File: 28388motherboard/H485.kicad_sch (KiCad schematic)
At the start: 23 parts, among them CN8 DB141V-2.54-6P, Q44 TPT75176B-SO1R, Q45 SN74LVC1G125DCKR

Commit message: 完成第一版引脚分配
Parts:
- removed D12, D34: ${MANUFACTURER PART}, 1mmlab_footprint:SOD-323_L1.8-W1.3-LS2.5-BI, symbol ESD:PESD12VL1BA,115
- added D20: SDT23C712L02_C5197393, Lib2ic:SOT-23-3_L2.9-W1.3-P1.90-LS2.4-BR, symbol sheet1-altium-import:SDT23C712L02_C5197393
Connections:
- net GND: now also D20.3
- net 485B: now reaches C181.1, L14.4, Q44.7 (B), R284.2, R296.1
- net 485B: now also D20.2
- net 485A: now reaches C182.1, L14.1, Q44.6 (A), R286.1, R296.2
- net 485A: now also D20.1

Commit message: 修改了一些bug，进行了一些布线
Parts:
- renumbered C170 to C25, C172 to C26, C174 to C27, C176 to C28, C179 to C29, C181 to C30, C182 to C31, CN8 to CN3, D20 to D14, L14 to L3, Q44 to Q10, Q45 to Q11, R272 to R34, R274 to R35, R276 to R36, R278 to R37, R281 to R38, R282 to R39, R284 to R40, R286 to R41, R295 to R42, R296 to R43

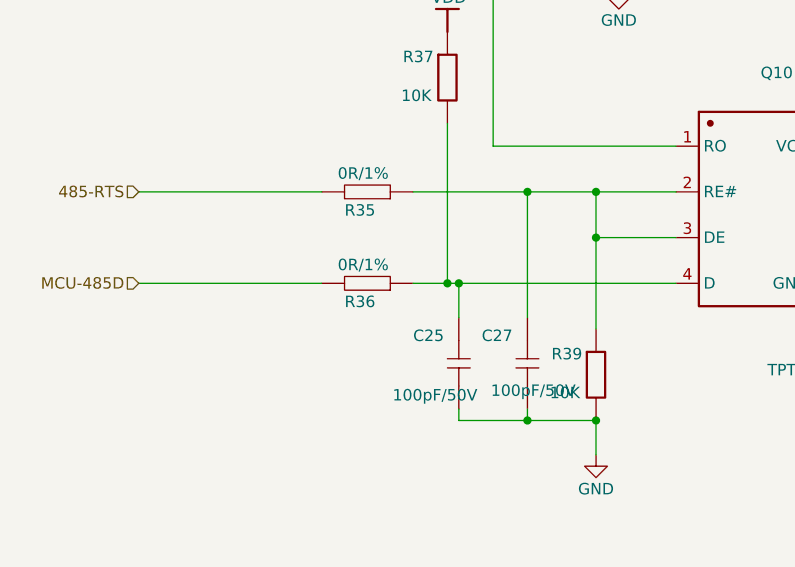
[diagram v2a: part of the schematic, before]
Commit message: 完成布局布线，需要丝印检查，原理图检查
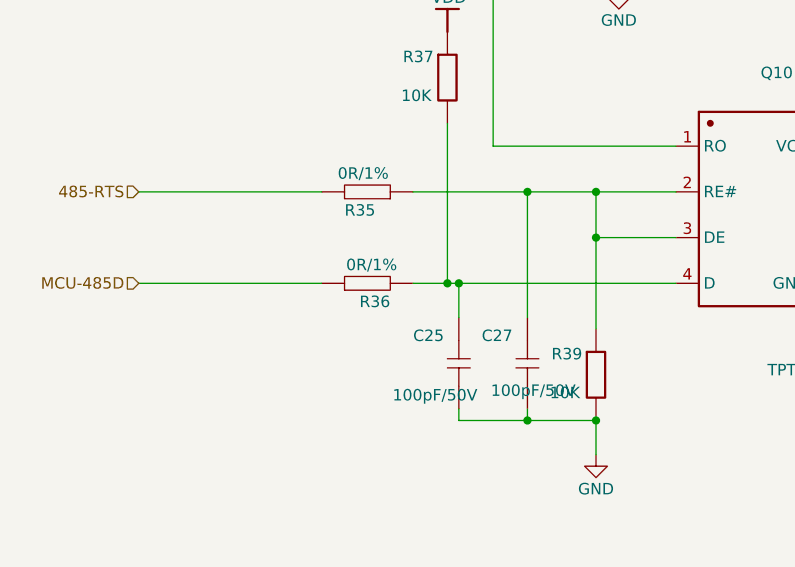
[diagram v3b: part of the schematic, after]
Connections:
- net MCU-485D: now also R36.1; no longer R36.2
- net at C25.1, Q10.4 (D), R37.2: now also R36.2; no longer R36.1
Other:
- moved on the sheet: R36
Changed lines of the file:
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@@
 	(wire
 		(pts
-			(xy 82.55 99.06) (xy 81.28 99.06)
-		)
-		(stroke
-			(width 0)
-			(type default)
-		)
-	)
-	(wire
-		(pts
 			(xy 115.57 48.26) (xy 100.33 48.26)
 		)
@@
 	(wire
 		(pts
+			(xy 81.28 99.06) (xy 82.55 99.06)
+		)
+		(stroke
+			(width 0)
+			(type default)
+		)
+	)
+	(wire
+		(pts
 			(xy 171.45 99.06) (xy 161.29 99.06)
 		)
@@
 	(symbol
 		(lib_id "sheet1-altium-import:RES_7")
-		(at 74.93 101.6 180)
+		(at 69.85 101.6 0)
+		(mirror x)
 		(unit 1)
 		(exclude_from_sim no)
@@
 		(dnp no)
 		(property "Reference" "R36"
-			(at 69.85 101.854 0)
+			(at 74.93 101.854 0)
 			(effects
 				(font
@@
 		)
 		(property "Value" "0R/1%"
-			(at 69.088 96.266 0)
+			(at 75.692 96.266 0)
 			(effects
 				(font
@@
 		)
 		(property "Footprint" "Resistor_SMD:R_0603_1608Metric"
-			(at 74.93 101.6 0)
+			(at 69.85 101.6 0)
 			(effects
 				(font
@@
 		)
 		(property "Datasheet" ""
-			(at 74.93 101.6 0)
+			(at 69.85 101.6 0)
 			(effects
 				(font
@@
 		)
 		(property "Description" ""
-			(at 74.93 101.6 0)
+			(at 69.85 101.6 0)
 			(effects
 				(font
@@
 		)
 		(property "Automotive" "AEC-Q200"
-			(at 74.93 101.6 90)
+			(at 69.85 101.6 90)
 			(effects
 				(font
@@
 		)
 		(property "Datasheet Link" "\\\\10.192.7.10\\Dianqu-CIS\\DATASHEET-New\\电阻\\YAGEO_AC_规格书.pdf"
-			(at 74.93 101.6 90)
+			(at 69.85 101.6 90)
 			(effects
 				(font
@@
 		)
 		(property "EBOM Description" "电阻-0R-±1%-1/10W-(-55~155℃)-车规-0603"
-			(at 74.93 101.6 90)
+			(at 69.85 101.6 90)
 			(effects
 				(font
@@
 		)
 		(property "Height" "0.55"
-			(at 74.93 101.6 90)
+			(at 69.85 101.6 90)
 			(effects
 				(font
@@
 		)
 		(property "ID" "245"
-			(at 74.93 101.6 90)
+			(at 69.85 101.6 90)
 			(effects
 				(font
@@
 		)
 		(property "Implementation Type" "<none>"
-			(at 74.93 101.6 90)
+			(at 69.85 101.6 90)
 			(effects
 				(font
@@
 		)
 		(property "New Part Number" "3.2.03.01.00250"
-			(at 74.93 101.6 90)
+			(at 69.85 101.6 90)
 			(effects
 				(font
@@
 		)
 		(property "Origin Footprint" "0603R"
-			(at 74.93 101.6 90)
+			(at 69.85 101.6 90)
 			(effects
 				(font
@@
 		)
 		(property "PCB Footprint" "0603R"
-			(at 74.93 101.6 90)
+			(at 69.85 101.6 90)
 			(effects
 				(font
@@
 		)
 		(property "Part State" "已认定"
-			(at 74.93 101.6 90)
+			(at 69.85 101.6 90)
 			(effects
 				(font
@@
 		)
 		(property "Part Type" "普通电阻"
-			(at 74.93 101.6 90)
+			(at 69.85 101.6 90)
 			(effects
 				(font
@@
 		)
 		(property "Power Pins Visible" "False"
-			(at 74.93 101.6 90)
+			(at 69.85 101.6 90)
 			(effects
 				(font
@@
 		)
 		(property "Primitive" "DEFAULT"
-			(at 74.93 101.6 90)
+			(at 69.85 101.6 90)
 			(effects
 				(font
@@
 		)
 		(property "Source Package" "RES"
-			(at 74.93 101.6 90)
+			(at 69.85 101.6 90)
 			(effects
 				(font
@@
 		)
 		(property "priority" "H"
-			(at 74.93 101.6 90)
+			(at 69.85 101.6 90)
 			(effects
 				(font
@@
 		)
 		(property "purpose" "通用"
-			(at 74.93 101.6 90)
+			(at 69.85 101.6 90)
 			(effects
 				(font
@@
 		)
 		(property "制造商名称" "MC000003_国巨（YAGEO）"
-			(at 74.93 101.6 90)
+			(at 69.85 101.6 90)
 			(effects
 				(font

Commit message: 1. 485 缺电源+5V 1 2. 标一下已用ADCforDCbus 1 3. 逆变器三相采样 coming soon 4. 电源灯 5V 3.3V 1 5. 测试点 1 6. 电源走线 需要人检查 7. 接口附近储能电容 1 8.
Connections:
- net D+5V: now also CN3.4
- net GND: no longer CN3.4
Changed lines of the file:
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@@
 	(paper "A4")
 	(junction
-		(at 233.68 96.52)
-		(diameter 0)
-		(color 0 0 0 0)
-	)
-	(junction
 		(at 176.53 99.06)
 		(diameter 0)
@@
 	(wire
 		(pts
-			(xy 233.68 96.52) (xy 233.68 104.14)
-		)
-		(stroke
-			(width 0)
-			(type default)
-		)
-	)
-	(wire
-		(pts
 			(xy 153.67 93.98) (xy 153.67 81.28)
 		)
@@
 	(wire
 		(pts
+			(xy 236.22 96.52) (xy 236.22 82.55)
+		)
+		(stroke
+			(width 0)
+			(type default)
+		)
+	)
+	(wire
+		(pts
 			(xy 227.33 93.98) (xy 227.33 95.25)
 		)
@@
 	(wire
 		(pts
-			(xy 78.74 53.34) (xy 78.74 60.96)
+			(xy 240.03 96.52) (xy 236.22 96.52)
 		)
 		(stroke
@@
 	(wire
 		(pts
-			(xy 204.47 99.06) (xy 204.47 95.25)
+			(xy 78.74 53.34) (xy 78.74 60.96)
 		)
 		(stroke
@@
 	(wire
 		(pts
-			(xy 233.68 96.52) (xy 240.03 96.52)
+			(xy 204.47 99.06) (xy 204.47 95.25)
 		)
 		(stroke
@@
 	(wire
 		(pts
-			(xy 233.68 91.44) (xy 233.68 96.52)
+			(xy 233.68 91.44) (xy 233.68 104.14)
 		)
 		(stroke
@@
 					(unit 1)
 				)
+			)
+		)
+	)
+	(symbol
+		(lib_id "sheet1-altium-import:D+5V")
+		(at 236.22 82.55 180)
+		(unit 1)
+		(exclude_from_sim no)
+		(in_bom yes)
+		(on_board yes)
+		(dnp no)
+		(property "Reference" "#PWR0308"
+			(at 236.22 82.55 0)
+			(effects
+				(font
+					(size 1.27 1.27)
+				)
+				(hide yes)
+			)
+		)
+		(property "Value" "D+5V"
+			(at 236.22 78.74 0)
+			(effects
+				(font
+					(size 1.27 1.27)
+				)
+			)
+		)
+		(property "Footprint" ""
+			(at 236.22 82.55 0)
+			(effects
+				(font
+					(size 1.27 1.27)
+				)
+				(hide yes)
+			)
+		)
+		(property "Datasheet" ""
+			(at 236.22 82.55 0)
+			(effects
+				(font
+					(size 1.27 1.27)
+				)
+				(hide yes)
+			)
+		)
+		(property "Description" "电源符号创建名为 'D+5V' 的全局标签"
+			(at 236.22 82.55 0)
+			(effects
+				(font
+					(size 1.27 1.27)
+				)
+				(hide yes)
+			)
+		)
+		(pin ""
+		)
+		(instances
+			(project "28388motherboard"
+				(path "/88c87a56-bf0e-49aa-812f-d0846700c8ff/30f612b7-5bdc-4c5b-9482-81b519ad00d6"
+					(reference "#PWR0308")
+					(unit 1)
+				)
+				(path "/88c87a56-bf0e-49aa-812f-d0846700c8ff/3ba8ca03-ed76-4c85-b19e-d2c90cb31384"
+					(reference "#PWR0310")
+					(unit 1)
+				)
+				(path "/88c87a56-bf0e-49aa-812f-d0846700c8ff/6c6142d1-0088-45dc-b843-44c9557b945c"
+					(reference "#PWR0312")
+					(unit 1)
+				)
+				(path "/88c87a56-bf0e-49aa-812f-d0846700c8ff/9f621359-c4a5-482e-a52e-bea19b45c818"
+					(reference "#PWR0311")
+					(unit 1)
+				)
